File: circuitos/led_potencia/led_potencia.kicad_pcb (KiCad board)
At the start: 2 copper layers, 115.2 x 91.5 mm, 67 parts, among them J1 Conn_01x02_Pin, J10 Conn_01x02_Pin, J11 Conn_01x02_Pin, J12 Conn_01x02_Pin, J13 Conn_01x02_Pin, J14 Conn_01x02_Pin, J15 Conn_01x02_Pin, J16 Conn_01x02_Pin, J17 Conn_01x02_Socket, J19 Conn_01x02_OE_GND, J2 Conn_01x02_Pin, J20 Conn_01x05_IN, J21 Conn_01x05_OUT, J3 Conn_01x02_Pin, J4 Conn_01x02_Pin, J5 Conn_01x02_Pin, J6 Conn_01x02_Pin, J7 Conn_01x02_Pin, J8 Conn_01x02_Pin, J9 Conn_01x02_Pin, Q1 IRLZ44N, Q18 IRF4905, Q19 IRF4905, Q2 IRLZ44N, Q20 IRF4905, Q21 PN2222A, Q22 PN2222A, Q23 PN2222A, Q24 IRF4905, Q25 PN2222A, Q3 IRLZ44N, Q4 IRLZ44N, U1 74HC595

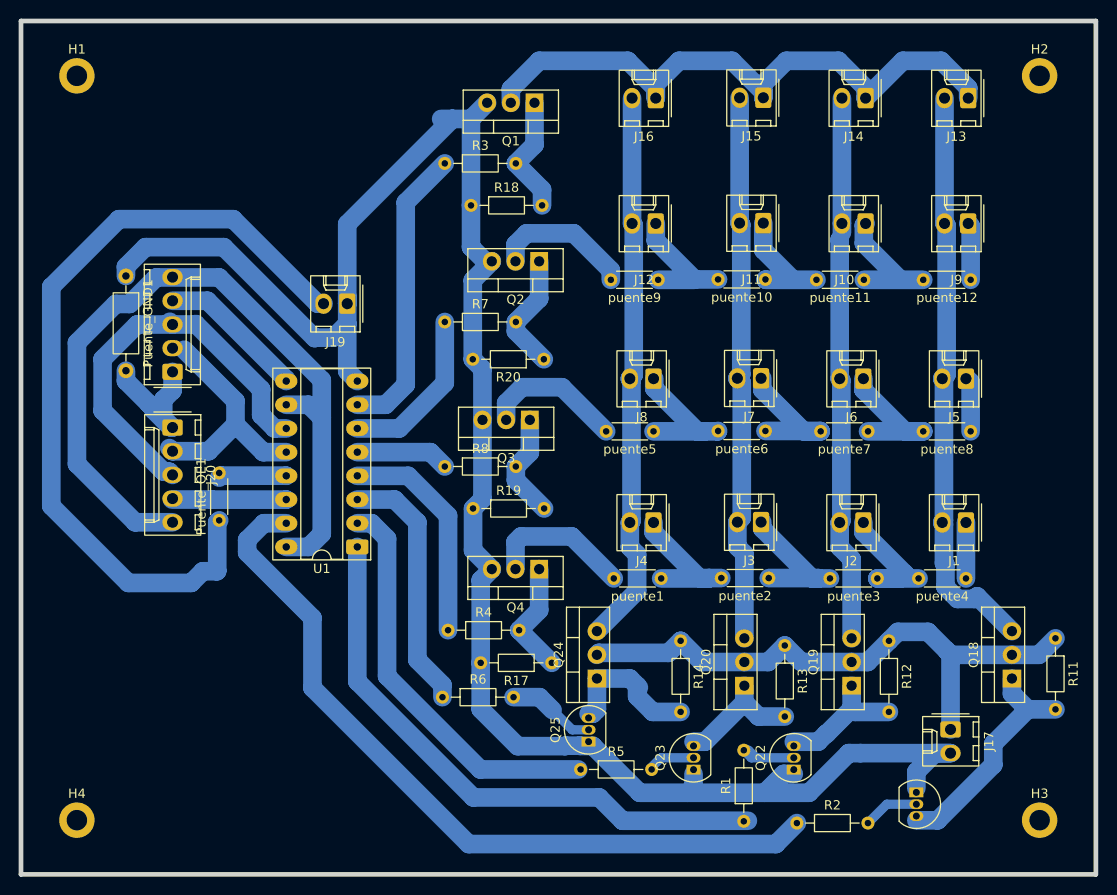
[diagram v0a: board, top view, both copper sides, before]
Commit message: achicando marggen por seguridad
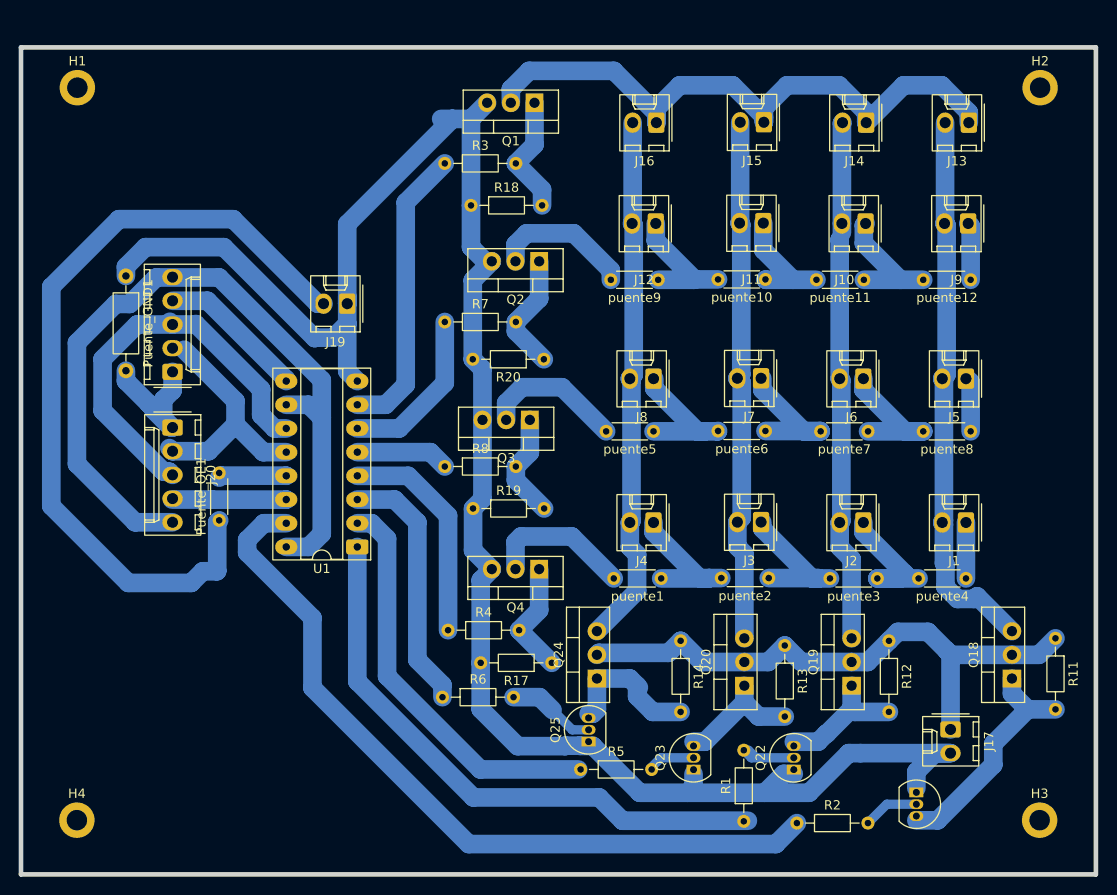
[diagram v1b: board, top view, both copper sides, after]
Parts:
- moved J13 2.63 mm to (152.4, 32.4)
- moved J14 2.63 mm to (141.4, 32.4)
- moved J15 2.63 mm to (130.4, 32.4)
- moved J16 2.63 mm to (118.9, 32.4)
- moved H2 1.27 mm to (160.0, 28.7)
- moved H1 1.27 mm to (56.8, 28.7)
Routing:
- net Net-(J1-Pin_2): track 62.3 -> 59.7 mm
- net Net-(J10-Pin_2): track 57.8 -> 55.2 mm
- net Net-(J12-Pin_2): track 59.7 -> 57.1 mm
- net Net-(J11-Pin_2): track 58.9 -> 56.3 mm
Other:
- board size 115.2 x 91.5 mm -> 115.2 x 88.7 mm
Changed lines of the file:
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@@
 	(footprint "Connector_Molex:Molex_KK-254_AE-6410-02A_1x02_P2.54mm_Vertical"
 		(layer "F.Cu")
-		(at 130.34 29.73 180)
+		(at 130.4036 32.3596 180)
 		(descr "Molex KK-254 Interconnect System, old/engineering part number: AE-6410-02A example for new part number: 22-27-2021, 2 Pins (http://www.molex.com/pdm_docs/sd/022272021_sd.pdf)")
 		(tags "connector Molex KK-254 vertical")
@@
 	(footprint "Connector_Molex:Molex_KK-254_AE-6410-02A_1x02_P2.54mm_Vertical"
 		(layer "F.Cu")
-		(at 141.31 29.77 180)
+		(at 141.3736 32.3996 180)
 		(descr "Molex KK-254 Interconnect System, old/engineering part number: AE-6410-02A example for new part number: 22-27-2021, 2 Pins (http://www.molex.com/pdm_docs/sd/022272021_sd.pdf)")
 		(tags "connector Molex KK-254 vertical")
@@
 	(footprint "MountingHole:MountingHole_2.2mm_M2_DIN965_Pad"
 		(layer "F.Cu")
-		(at 159.9692 27.3812)
+		(at 160.02 28.6512)
 		(descr "Mounting Hole 2.2mm, M2, generated by kicad-footprint-generator mountinghole.py")
 		(tags "mountinghole M2 DIN965")
@@
 	(footprint "Connector_Molex:Molex_KK-254_AE-6410-02A_1x02_P2.54mm_Vertical"
 		(layer "F.Cu")
-		(at 118.81 29.77 180)
+		(at 118.8736 32.3996 180)
 		(descr "Molex KK-254 Interconnect System, old/engineering part number: AE-6410-02A example for new part number: 22-27-2021, 2 Pins (http://www.molex.com/pdm_docs/sd/022272021_sd.pdf)")
 		(tags "connector Molex KK-254 vertical")
@@
 	(footprint "Connector_Molex:Molex_KK-254_AE-6410-02A_1x02_P2.54mm_Vertical"
 		(layer "F.Cu")
-		(at 152.31 29.77 180)
+		(at 152.3736 32.3996 180)
 		(descr "Molex KK-254 Interconnect System, old/engineering part number: AE-6410-02A example for new part number: 22-27-2021, 2 Pins (http://www.molex.com/pdm_docs/sd/022272021_sd.pdf)")
 		(tags "connector Molex KK-254 vertical")
@@
 	(footprint "MountingHole:MountingHole_2.2mm_M2_DIN965_Pad"
 		(layer "F.Cu")
-		(at 56.7436 27.3812)
+		(at 56.7944 28.6512)
 		(descr "Mounting Hole 2.2mm, M2, generated by kicad-footprint-generator mountinghole.py")
 		(tags "mountinghole M2 DIN965")
@@
 	)
 	(gr_rect
-		(start 50.75 21.5)
+		(start 50.75 24.3332)
 		(end 166 113)
 		(stroke
@@
 	)
 	(segment
+		(start 149.8336 43.1464)
+		(end 149.77 43.21)
+		(width 2)
+		(layer "B.Cu")
+		(net "Net-(J1-Pin_2)")
+	)
+	(segment
 		(start 150 59.38)
 		(end 149.53 59.85)
@@
 	)
 	(segment
+		(start 149.8336 32.3996)
+		(end 149.8336 43.1464)
+		(width 2)
+		(layer "B.Cu")
+		(net "Net-(J1-Pin_2)")
+	)
+	(segment
 		(start 153.265635 83.185635)
 		(end 157 86.92)
@@
 	)
 	(segment
-		(start 149.77 29.77)
-		(end 149.77 43.21)
-		(width 2)
-		(layer "B.Cu")
-		(net "Net-(J1-Pin_2)")
-	)
-	(segment
 		(start 150 43.44)
 		(end 150 59.38)
@@
 	)
 	(segment
-		(start 115.81 25.77)
-		(end 118.81 28.77)
+		(start 130.4036 30.8696)
+		(end 132.8736 28.3996)
 		(width 2)
 		(layer "B.Cu")
@@
 	)
 	(segment
-		(start 103.27 28.81)
-		(end 106.31 25.77)
+		(start 118.8736 30.8996)
+		(end 121.3736 28.3996)
 		(width 2)
 		(layer "B.Cu")
@@
 	)
 	(segment
-		(start 130.34 28.24)
-		(end 132.81 25.77)
+		(start 145.3736 28.3996)
+		(end 149.4686 28.3996)
 		(width 2)
 		(layer "B.Cu")
@@
 	)
 	(segment
-		(start 118.81 28.27)
-		(end 121.31 25.77)
+		(start 149.4686 28.3996)
+		(end 152.3736 31.3046)
 		(width 2)
 		(layer "B.Cu")
@@
 	)
 	(segment
-		(start 103.27 30.27)
-		(end 103.27 28.81)
+		(start 118.8736 31.3996)
+		(end 118.8736 32.3996)
 		(width 2)
 		(layer "B.Cu")
@@
 	)
 	(segment
-		(start 145.31 25.77)
-		(end 149.405 25.77)
+		(start 141.3736 31.3046)
+		(end 141.3736 32.3996)
 		(width 2)
 		(layer "B.Cu")
@@
 	)
 	(segment
-		(start 149.405 25.77)
-		(end 152.31 28.675)
+		(start 130.4036 31.747178)
+		(end 130.4036 32.3596)
 		(width 2)
 		(layer "B.Cu")
@@
 	)
 	(segment
-		(start 141.31 28.675)
-		(end 141.31 29.77)
+		(start 103.27 30.27)
+		(end 103.27 28.81)
 		(width 2)
 		(layer "B.Cu")
@@
 	)
 	(segment
-		(start 130.34 29.117578)
-		(end 130.34 29.73)
+		(start 118.8736 32.3996)
+		(end 118.8736 30.8996)
 		(width 2)
 		(layer "B.Cu")
@@
 	)
 	(segment
-		(start 118.81 29.77)
-		(end 118.81 28.27)
+		(start 127.056022 28.3996)
+		(end 130.4036 31.747178)
 		(width 2)
 		(layer "B.Cu")
@@
 	)
 	(segment
-		(start 118.81 28.77)
-		(end 118.81 29.77)
+		(start 152.3736 31.3046)
+		(end 152.3736 32.3996)
 		(width 2)
 		(layer "B.Cu")
@@
 	)
 	(segment
-		(start 126.992422 25.77)
-		(end 130.34 29.117578)
+		(start 130.4036 32.3596)
+		(end 130.4036 30.8696)
 		(width 2)
 		(layer "B.Cu")
@@
 	)
 	(segment
-		(start 152.31 28.675)
-		(end 152.31 29.77)
+		(start 132.8736 28.3996)
+		(end 138.4686 28.3996)
 		(width 2)
 		(layer "B.Cu")
@@
 	)
 	(segment
-		(start 130.34 29.73)
-		(end 130.34 28.24)
+		(start 103.27 28.81)
+		(end 105.2322 26.8478)
 		(width 2)
 		(layer "B.Cu")
@@
 	)
 	(segment
-		(start 132.81 25.77)
-		(end 138.405 25.77)
+		(start 105.2322 26.8478)
+		(end 114.3218 26.8478)
 		(width 2)
 		(layer "B.Cu")
@@
 	)
 	(segment
-		(start 106.31 25.77)
-		(end 115.81 25.77)
+		(start 114.3218 26.8478)
+		(end 118.8736 31.3996)
 		(width 2)
 		(layer "B.Cu")
@@
 	)
 	(segment
-		(start 121.31 25.77)
-		(end 126.992422 25.77)
+		(start 121.3736 28.3996)
+		(end 127.056022 28.3996)
 		(width 2)
 		(layer "B.Cu")
@@
 	)
 	(segment
-		(start 141.31 29.77)
-		(end 145.31 25.77)
+		(start 141.3736 32.3996)
+		(end 145.3736 28.3996)
 		(width 2)
 		(layer "B.Cu")
@@
 	)
 	(segment
-		(start 138.405 25.77)
-		(end 141.31 28.675)
+		(start 138.4686 28.3996)
+		(end 141.3736 31.3046)
 		(width 2)
 		(layer "B.Cu")
@@
 	)
 	(segment
+		(start 127.8636 43.1064)
+		(end 127.8 43.17)
+		(width 2)
+		(layer "B.Cu")
+		(net "Net-(J11-Pin_2)")
+	)
+	(segment
 		(start 127.56 77.875)
 		(end 128.31 78.625)
@@
 	)
 	(segment
-		(start 127.8 29.73)
-		(end 127.8 43.17)
+		(start 127.8636 32.3596)
+		(end 127.8636 43.1064)
 		(width 2)
 		(layer "B.Cu")
@@
 	)
 	(segment
+		(start 138.77 32.4632)
+		(end 138.8336 32.3996)
+		(width 2)
+		(layer "B.Cu")
+		(net "Net-(J10-Pin_2)")
+	)
+	(segment
 		(start 138.53 77.915)
 		(end 138.53 75.27)
@@
 	(segment
 		(start 138.77 43.21)
-		(end 138.77 29.77)
+		(end 138.77 32.4632)
 		(width 2)
 		(layer "B.Cu")
@@
 	)
 	(segment
-		(start 116.27 43.21)
-		(end 116.27 29.77)
-		(width 2)
-		(layer "B.Cu")
-		(net "Net-(J12-Pin_2)")
-	)
-	(segment
 		(start 116.45 43.39)
 		(end 116.27 43.21)
@@
 		(width 2)
 		(layer "B.Cu")
+		(net "Net-(J12-Pin_2)")
+	)
+	(segment
+		(start 116.3336 43.1464)
+		(end 116.27 43.21)
+		(width 2)
+		(layer "B.Cu")
+		(net "Net-(J12-Pin_2)")
+	)
+	(segment
+		(start 116.3336 32.3996)
+		(end 116.3336 43.1464)
+		(width 2)
+		(layer "B.Cu")

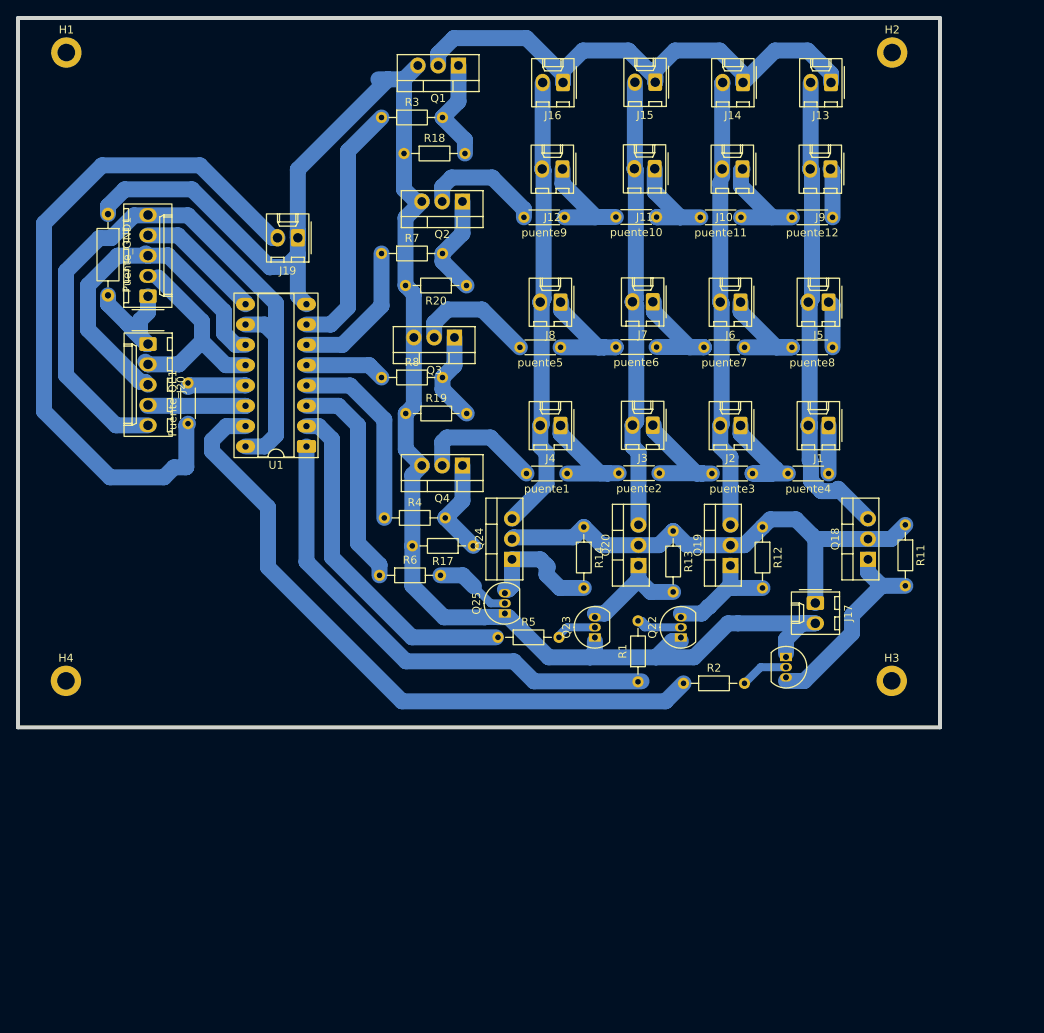
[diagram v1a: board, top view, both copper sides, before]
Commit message: relleno gnd
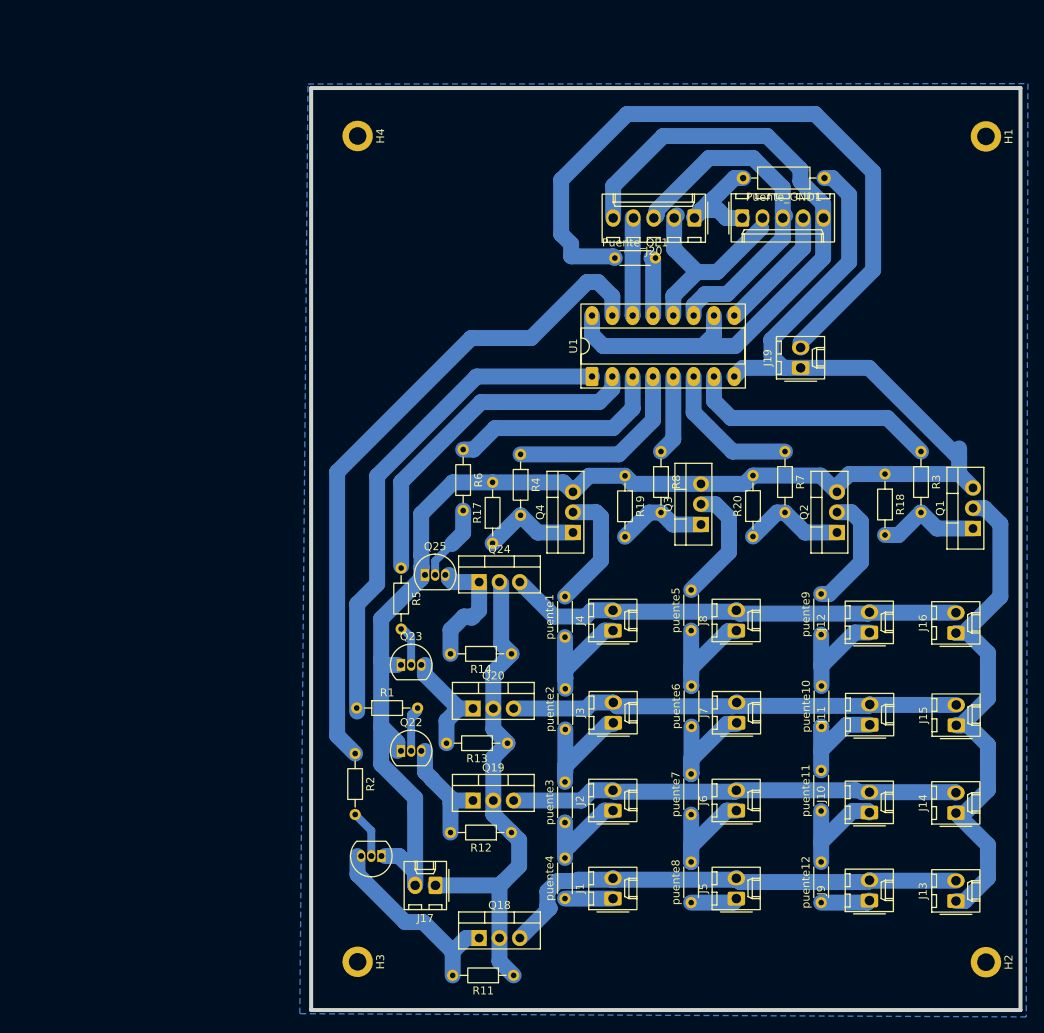
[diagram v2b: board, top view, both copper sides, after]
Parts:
- moved H1 115.4 mm to (171.7, 39.1), turned to -90 degrees
- moved H2 114.3 mm to (171.7, 142.4), turned to -90 degrees
- moved J13 103.5 mm to (168.0, 134.7), turned to 90 degrees
- moved J14 95.1 mm to (168.0, 123.7), turned to 90 degrees
- moved J9 91.6 mm to (157.2, 134.6), turned to 90 degrees
- moved Puente_GND1 89.7 mm to (151.6, 44.3), turned to 180 degrees
- moved J15 88.8 mm to (168.0, 112.7), turned to 90 degrees
- moved Q1 86.5 mm to (170.1, 88.1), turned to 90 degrees
- moved puente12 85.7 mm to (151.1, 134.9), turned to 90 degrees
- moved J16 84.5 mm to (168.0, 101.2), turned to 90 degrees
- moved J10 82.0 mm to (157.2, 123.6), turned to 90 degrees
- moved R3 79.3 mm to (163.6, 78.5), turned to -90 degrees
- moved H4 77.3 mm to (93.2, 39.1), turned to -90 degrees
- moved J5 75.4 mm to (140.5, 134.4), turned to 90 degrees
- moved H3 75.4 mm to (93.2, 142.3), turned to -90 degrees
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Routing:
- added copper zone on B.Cu, net GND
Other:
- board size 115.2 x 88.7 mm -> 88.7 x 115.2 mm
